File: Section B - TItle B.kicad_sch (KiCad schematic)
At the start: 0 parts

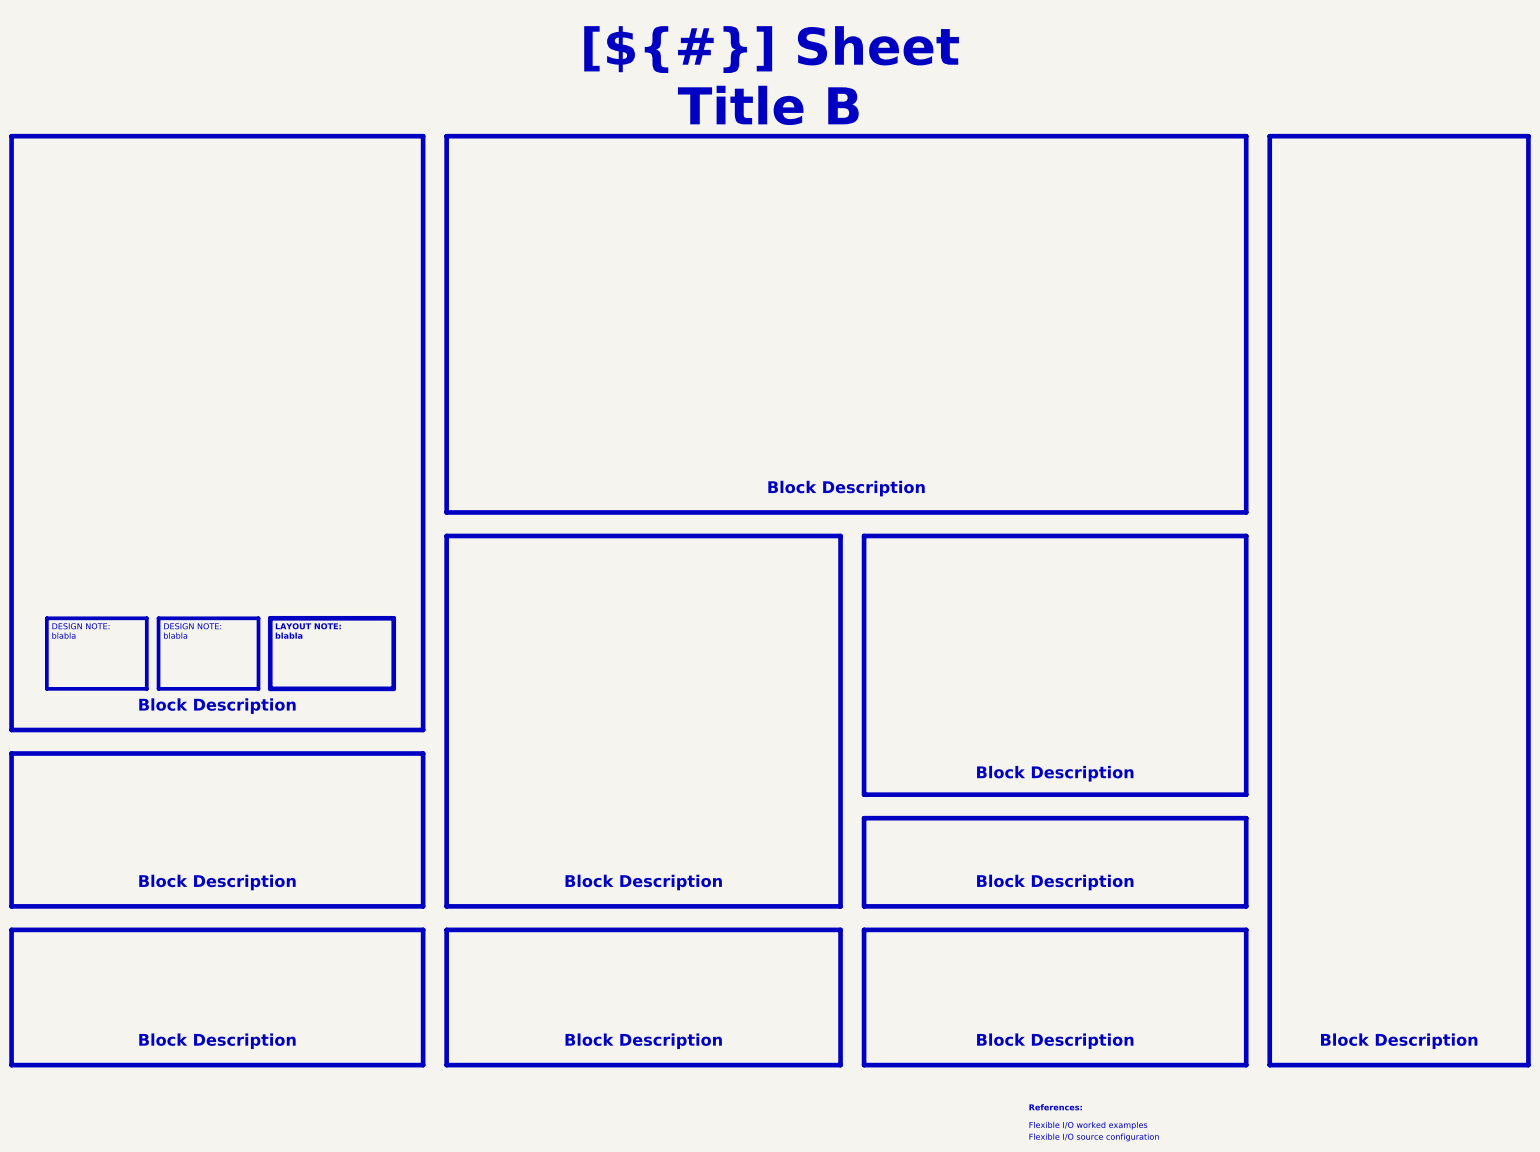
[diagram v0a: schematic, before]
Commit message: Initial commit: Moved over previous design and added isolation to CAN bus.
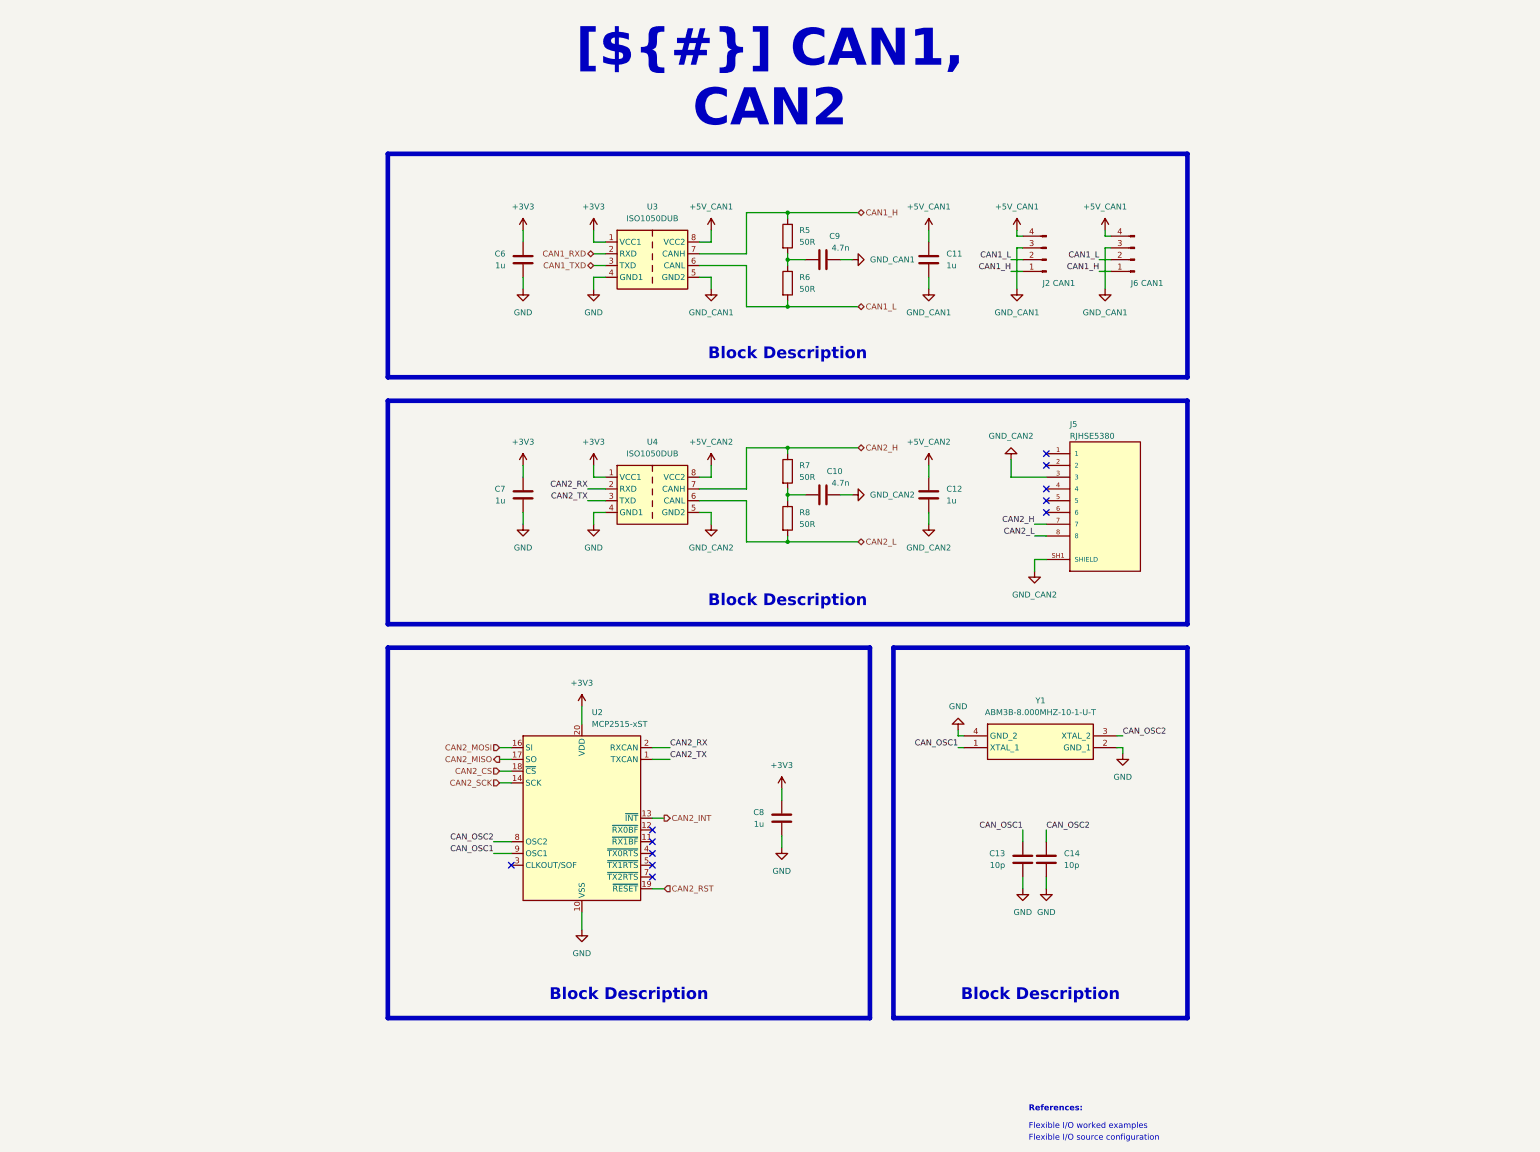
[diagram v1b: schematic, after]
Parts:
- added C10, C9: 4.7n, Capacitor_SMD:C_0603_1608Metric_Pad1.08x0.95mm_HandSolder, symbol Device:C
- added C11, C12, C6, C7, C8: 1u, Capacitor_SMD:C_0603_1608Metric_Pad1.08x0.95mm_HandSolder, symbol Device:C
- added C13, C14: 10p, Capacitor_SMD:C_0603_1608Metric_Pad1.08x0.95mm_HandSolder, symbol Device:C
- added J2, J6: CAN1, Connector_JST:JST_XH_S4B-XH-A_1x04_P2.50mm_Horizontal, symbol Connector:Conn_01x04_Pin
- added J5: RJHSE5380, RJHSE5380:AMPHENOL_RJHSE5380, symbol RJHSE5380:RJHSE5380
- added R5, R6, R7, R8: 50R, Resistor_SMD:R_0603_1608Metric_Pad0.98x0.95mm_HandSolder, symbol Device:R
- added U2: MCP2515-xST, Package_SO:TSSOP-20_4.4x6.5mm_P0.65mm, symbol Interface_CAN_LIN:MCP2515-xST
- added U3, U4: ISO1050DUB, Package_SO:SOP-8_6.62x9.15mm_P2.54mm, symbol Interface_CAN_LIN:ISO1050DUB
- added Y1: ABM3B-8.000MHZ-10-1-U-T, ABM3B-8.000MHZ-10-1-U-T:ABM3B, symbol ABM3B-8_000MHZ-10-1-U-T:ABM3B-8.000MHZ-10-1-U-T
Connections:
- new net: C10.1, R7.2, R8.1
- new net: C9.1, R5.2, R6.1
- new net +3V3: C6.1, C7.1, C8.1, U2.20 (VDD), U3.1 (VCC1), U4.1 (VCC1)
- new net +5V_CAN1: C11.1, J2.4 (Pin_4), J6.4 (Pin_4), U3.8 (VCC2)
- new net +5V_CAN2: C12.1, U4.8 (VCC2)
- new net CAN1_H: J2.1 (Pin_1), J6.1 (Pin_1), R5.1, U3.7 (CANH)
- new net CAN1_L: J2.2 (Pin_2), J6.2 (Pin_2), R6.2, U3.6 (CANL)
- new net CAN1_RXD: U3.2 (RXD)
- new net CAN1_TXD: U3.3 (TXD)
- new net CAN2_CS: U2.18 (~{CS})
- new net CAN2_H: J5.7, R7.1, U4.7 (CANH)
- new net CAN2_INT: U2.13 (~{INT})
- new net CAN2_L: J5.8, R8.2, U4.6 (CANL)
- new net CAN2_MISO: U2.17 (SO)
- new net CAN2_MOSI: U2.16 (SI)
- new net CAN2_RST: U2.19 (~{RESET})
- new net CAN2_RX: U2.2 (RXCAN), U4.2 (RXD)
- new net CAN2_SCK: U2.14 (SCK)
- new net CAN2_TX: U2.1 (TXCAN), U4.3 (TXD)
- new net CAN_OSC1: C13.1, U2.9 (OSC1), Y1.1 (XTAL_1)
- new net CAN_OSC2: C14.1, U2.8 (OSC2), Y1.3 (XTAL_2)
- new net GND: C13.2, C14.2, C6.2, C7.2, C8.2, U2.10 (VSS), U3.4 (GND1), U4.4 (GND1), Y1.2 (GND_1), Y1.4 (GND_2)
- new net GND_CAN1: C11.2, C9.2, J2.3 (Pin_3), J6.3 (Pin_3), U3.5 (GND2)
- new net GND_CAN2: C10.2, C12.2, J5.3, J5.SH1 (SHIELD), J5.SH2 (SHIELD), U4.5 (GND2)
- no-connect marks 0 -> 11
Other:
- title: Sheet Title B -> CAN1, CAN2
